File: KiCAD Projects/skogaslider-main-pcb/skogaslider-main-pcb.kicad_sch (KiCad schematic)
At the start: 183 parts, among them J1 USB_C_Receptacle_USB2.0, J2 USB_C_Receptacle_USB2.0, J3 Conn_01x03, J4 Conn_02x16_Top_Bottom, J5 HDMI_A_No_Video, J6 HDMI_A_No_Video, Q1 BSS138, SW1 SW_Push, SW2 SW_Push, SW3 SW_Push, SW4 SW_Push, U1 NCP1117-3.3_SOT223, U2 MPR121QR2, U3 MPR121QR2, U4 USBLC6-2P6, U5 RP2040, U6 M24C02-RMN, U7 W25Q128JVS, U8 MPR121QR2, U9 74HC4051, Y1 ABLS-12.000MHZ-B4-T

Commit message: New revision of the mainboard schematic and layout. Switched the air towers from HDMI to USB-C, and made them use the I2C bus for communication to reduce the number of pins
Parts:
- removed C57: 100nF, Capacitor_SMD:C_0402_1005Metric, symbol Device:C_Small
- removed H1, H10, H11, H12, H2, H3, H4, H5, H6, H7, H8, H9: MountingHole, MountingHole:MountingHole_3.2mm_M3, symbol Mechanical:MountingHole
- removed J5, J6: HDMI_A_No_Video, Skogaslider_Custom_Footprints:HDMI_Connector_SMD, symbol Skogaslider_Custom_Symbols:HDMI_A_No_Video
- removed R24: 10k, Resistor_SMD:R_0603_1608Metric, symbol Device:R
- removed SW1, SW2, SW3, SW4: SW_Push, TS-1187A-B-A-B:SW_TS-1187A-B-A-B, symbol Switch:SW_Push
- removed TP1, TP2, TP3, TP4: TestPoint, TestPoint:TestPoint_Pad_D1.5mm, symbol Connector:TestPoint
- removed U9: 74HC4051, Package_SO:TSSOP-16_4.4x5mm_P0.65mm, symbol 74xx:74HC4051
- added H1, H10, H2, H3, H4, H5, H6, H9: MountingHole_Pad, MountingHole:MountingHole_3.2mm_M3_DIN965_Pad_TopBottom, symbol Mechanical:MountingHole_Pad
- added J5, J6: USB_C_Receptacle_USB2.0, Connector_USB:USB_C_Receptacle_HRO_TYPE-C-31-M-12, symbol Connector:USB_C_Receptacle_USB2.0
- added S1: TS-1187A-B-A-B, TS-1187A-B-A-B:TS1187ABAB, symbol TS-1187A-B-A-B:TS-1187A-B-A-B
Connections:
- net +5V: now also R12.1, J5.A4 (VBUS), J5.A9 (VBUS), J5.B4 (VBUS), J5.B9 (VBUS), J6.A4 (VBUS), J6.A9 (VBUS), J6.B4 (VBUS), J6.B9 (VBUS)
- net GND: now also J5.A1 (GND), J5.A12 (GND), J5.B1 (GND), J5.B12 (GND), J5.S1 (SHIELD), J6.A1 (GND), J6.A12 (GND), J6.B1 (GND), J6.B12 (GND), J6.S1 (SHIELD), S1.C1 (NO_1), S1.D1 (NO_2)
- net RIGHT_RGB_DO: now also J5.A6 (D+), J5.B6 (D+), J6.A6 (D+), J6.B6 (D+)
- net SCL: now also J5.A5 (CC1), J5.B5 (CC2), J6.A5 (CC1), J6.B5 (CC2)
- net SDA: now also J5.A8 (SBU1), J5.B8 (SBU2), J6.A8 (SBU1), J6.B8 (SBU2)
- net SLIDER_RGB_DO: now also J6.A7 (D-), J6.B7 (D-)
- net ~{USB_BOOT}: now also S1.A1 (COM_1), S1.B1 (COM_2)
- net at D2.2 (A), J1.A4 (VBUS), J1.A9 (VBUS)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: no longer R12.1
- net AIR_LED_0: no longer names the net of U5.14 (GPIO11)
- net AIR_LED_1: no longer names the net of U5.17 (GPIO14)
- net AIR_LED_2: no longer names the net of U5.13 (GPIO10)
- net AIR_LED_3: no longer names the net of U5.16 (GPIO13)
- net AIR_LED_4: no longer names the net of U5.12 (GPIO9)
- net AIR_LED_5: no longer names the net of U5.15 (GPIO12)
- net AIR_SENSOR_IN: no longer names the net of U5.38 (GPIO26_ADC0)
- net MUX_0: no longer names the net of U5.27 (GPIO16)
- net MUX_1: no longer names the net of U5.28 (GPIO17)
- net MUX_2: no longer names the net of U5.29 (GPIO18)
- net SW_FUNCTION: no longer names the net of U5.11 (GPIO8)
- net SW_SVC: no longer names the net of U5.9 (GPIO7)
- net SW_TEST: no longer names the net of U5.8 (GPIO6)
- no-connect marks 36 -> 51
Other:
- note removed: "Air Sensor Multiplexer"
- note removed: "Function Buttons"
- moved on the sheet: C23, C24, D2, R12, R14, R23, Y1

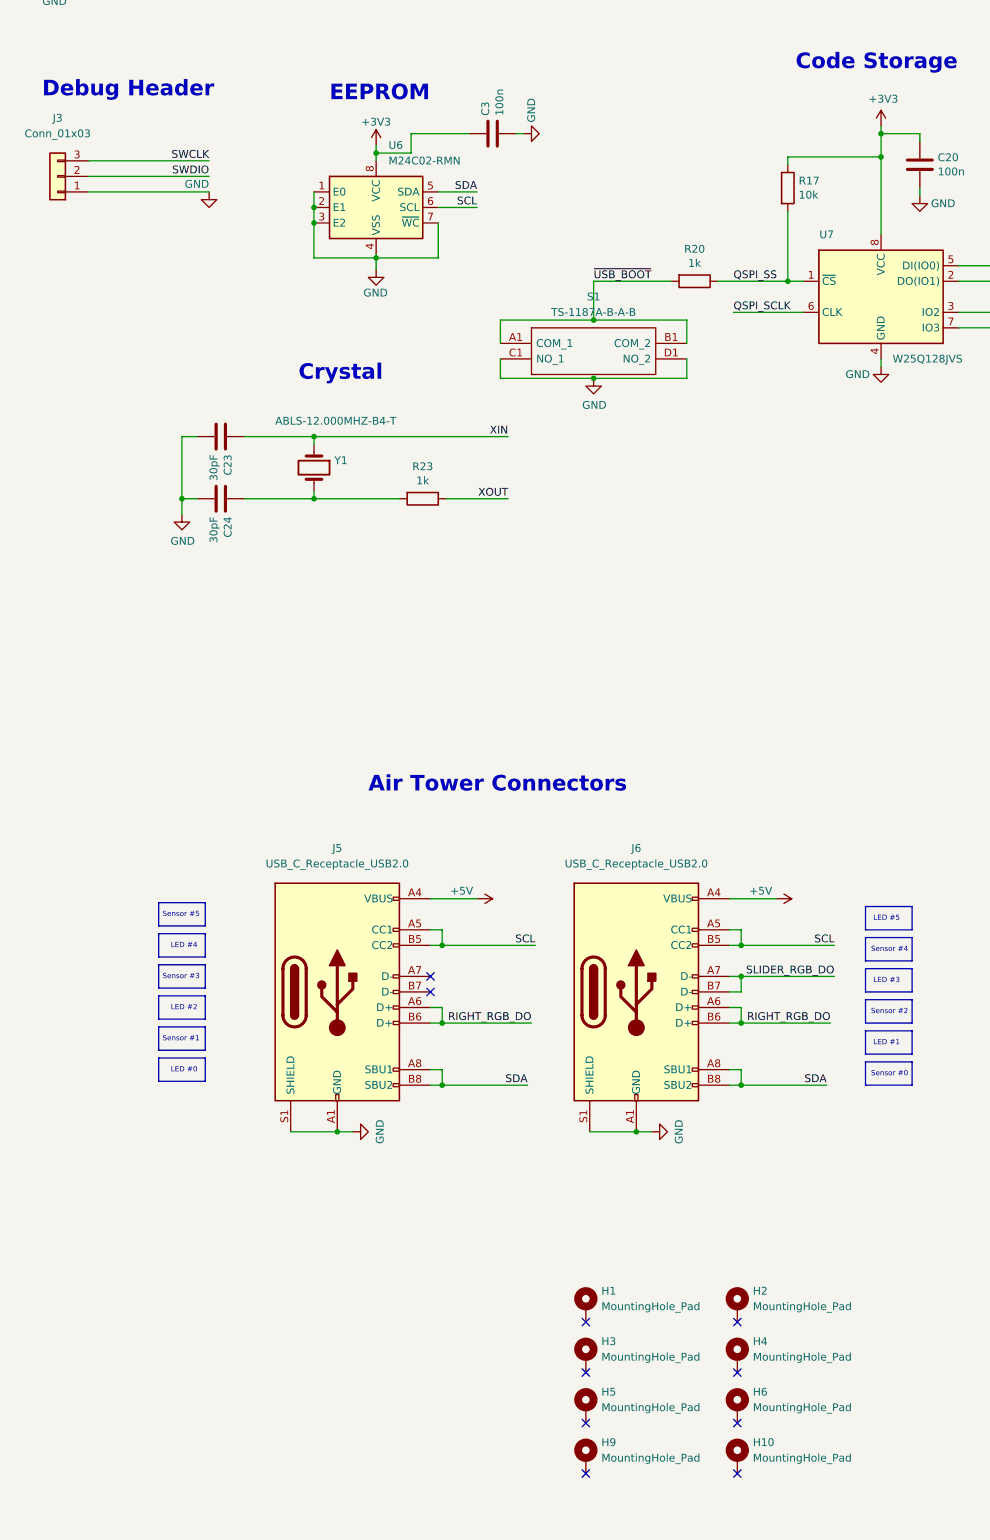
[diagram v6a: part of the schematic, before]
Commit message: Fix up the top edge of the board so it fits within the controller CAD, and add more mounting holes.
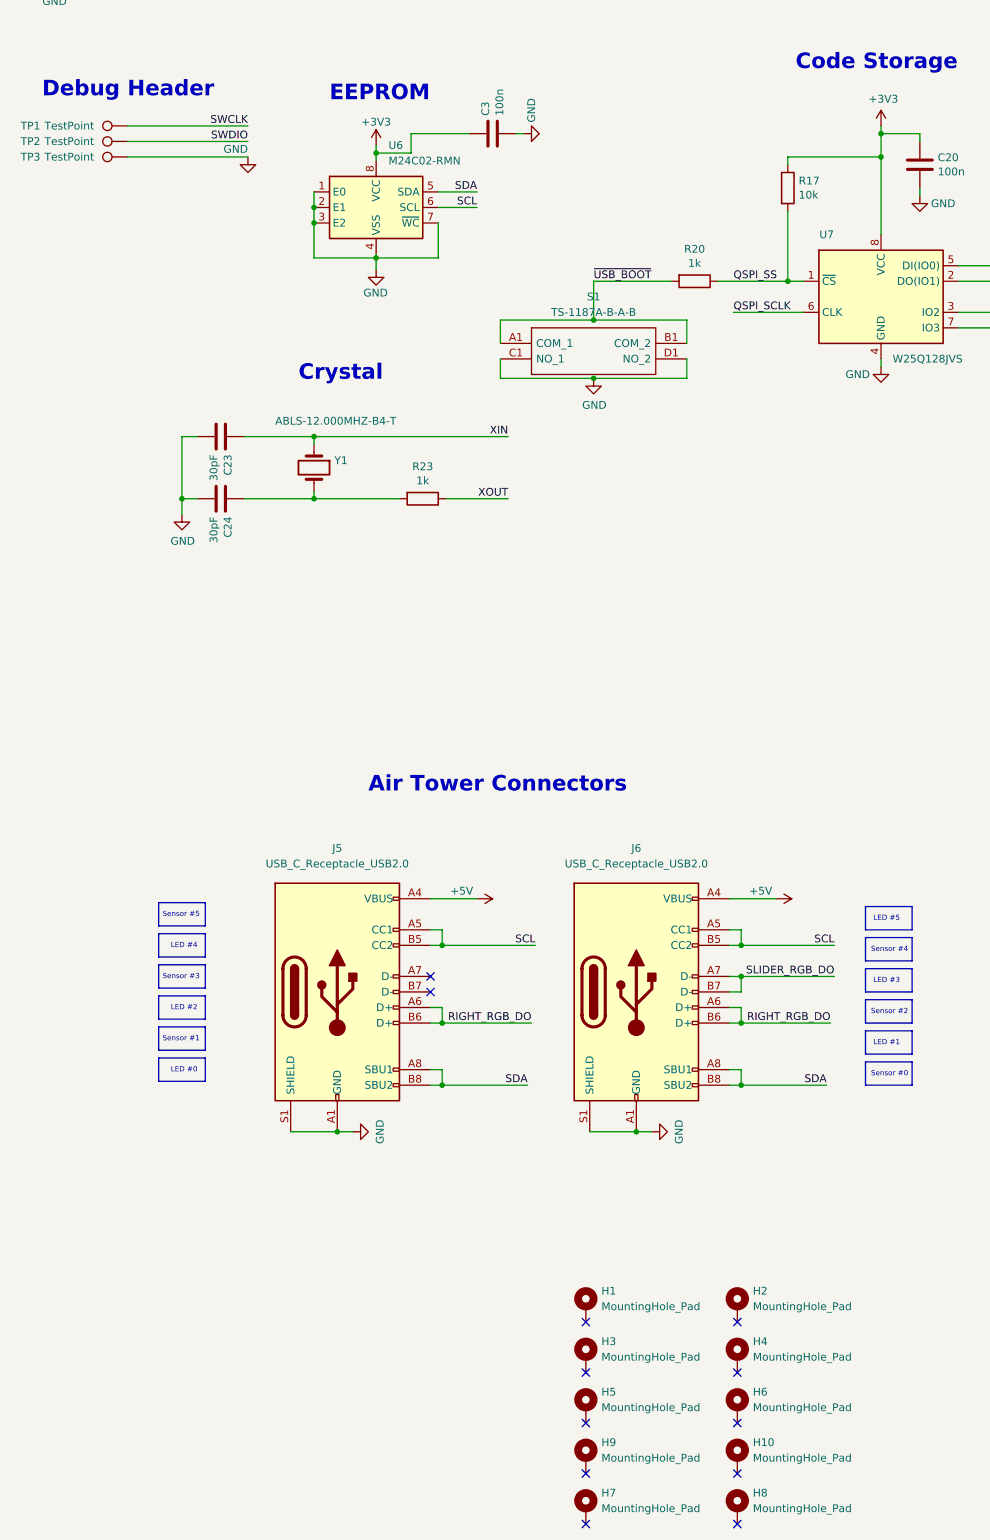
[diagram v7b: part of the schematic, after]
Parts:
- removed J3: Conn_01x03, Connector_PinHeader_2.54mm:PinHeader_1x03_P2.54mm_Vertical, symbol Connector_Generic:Conn_01x03
- added H7, H8: MountingHole_Pad, MountingHole:MountingHole_3.2mm_M3_DIN965_Pad_TopBottom, symbol Mechanical:MountingHole_Pad
- added TP1, TP2, TP3: TestPoint, TestPoint:TestPoint_Pad_1.0x1.0mm, symbol Connector:TestPoint
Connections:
- net GND: now also TP3.1
- net SWCLK: now also TP1.1
- net SWDIO: now also TP2.1
- no-connect marks 51 -> 53
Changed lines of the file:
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@@
   (no_connect (at 287.02 88.265))
   (no_connect (at 398.145 142.24))
+  (no_connect (at 109.22 341.63))
   (no_connect (at 399.415 63.5))
   (no_connect (at 134.62 53.975))
@@
   (no_connect (at 287.02 128.905))
   (no_connect (at 287.02 131.445))
+  (no_connect (at 133.985 341.63))
   (no_connect (at 487.045 63.5))
   (no_connect (at 133.985 308.61))
@@
     (stroke (width 0) (type default) (color 0 0 0 0))
   )
-  (wire (pts (xy 27.94 123.825) (xy 47.625 123.825))
+  (wire (pts (xy 34.29 118.11) (xy 53.975 118.11))
     (stroke (width 0) (type default) (color 0 0 0 0))
   )
@@
     (stroke (width 0) (type default) (color 0 0 0 0))
   )
-  (wire (pts (xy 27.94 118.745) (xy 47.625 118.745))
+  (wire (pts (xy 34.29 113.03) (xy 53.975 113.03))
     (stroke (width 0) (type default) (color 0 0 0 0))
   )
@@
     (stroke (width 0) (type default) (color 0 0 0 0))
   )
-  (wire (pts (xy 27.94 121.285) (xy 47.625 121.285))
+  (wire (pts (xy 34.29 115.57) (xy 53.975 115.57))
     (stroke (width 0) (type default) (color 0 0 0 0))
   )
@@
     (effects (font (size 1.27 1.27)) (justify right bottom))
   )
-  (label "SWCLK" (at 47.625 118.745 180)
+  (label "SWCLK" (at 53.975 113.03 180)
     (effects (font (size 1.27 1.27)) (justify right bottom))
   )
@@
     (effects (font (size 1.27 1.27)) (justify right bottom))
   )
-  (label "SWDIO" (at 47.625 121.285 180)
+  (label "SWDIO" (at 53.975 115.57 180)
     (effects (font (size 1.27 1.27)) (justify right bottom))
   )
@@
     (pin "2")
   )
-  (symbol (lib_id "power:GND") (at 47.625 123.825 0) (unit 1)
+  (symbol (lib_id "power:GND") (at 53.975 118.11 0) (unit 1)
     (in_bom yes) (on_board yes)
-    (property "Reference" "#PWR031" (id 0) (at 47.625 130.175 0)
+    (property "Reference" "#PWR031" (id 0) (at 53.975 124.46 0)
       (effects (font (size 1.27 1.27)) hide)
     )
-    (property "Value" "GND" (id 1) (at 47.625 122.555 0)
+    (property "Value" "GND" (id 1) (at 53.975 116.84 0)
       (effects (font (size 1.27 1.27)) (justify right))
     )
-    (property "Footprint" "" (id 2) (at 47.625 123.825 0)
+    (property "Footprint" "" (id 2) (at 53.975 118.11 0)
       (effects (font (size 1.27 1.27)) hide)
     )
-    (property "Datasheet" "" (id 3) (at 47.625 123.825 0)
+    (property "Datasheet" "" (id 3) (at 53.975 118.11 0)
       (effects (font (size 1.27 1.27)) hide)
     )
@@
     (pin "2")
   )
+  (symbol (lib_id "Connector:TestPoint") (at 34.29 115.57 90) (unit 1)
+    (in_bom yes) (on_board yes)
+    (property "Reference" "TP2" (id 0) (at 18.415 115.57 90))
+    (property "Value" "TestPoint" (id 1) (at 24.765 115.57 90))
+    (property "Footprint" "TestPoint:TestPoint_Pad_1.0x1.0mm" (id 2) (at 34.29 110.49 0)
+      (effects (font (size 1.27 1.27)) hide)
+    )
+    (property "Datasheet" "~" (id 3) (at 34.29 110.49 0)
+      (effects (font (size 1.27 1.27)) hide)
+    )
+    (pin "1")
+  )
   (symbol (lib_id "Device:C") (at 210.82 262.89 0) (unit 1)
     (in_bom yes) (on_board yes)
@@
     (pin "2")
   )
+  (symbol (lib_id "Connector:TestPoint") (at 34.29 118.11 90) (unit 1)
+    (in_bom yes) (on_board yes)
+    (property "Reference" "TP3" (id 0) (at 18.415 118.11 90))
+    (property "Value" "TestPoint" (id 1) (at 24.765 118.11 90))
+    (property "Footprint" "TestPoint:TestPoint_Pad_1.0x1.0mm" (id 2) (at 34.29 113.03 0)
+      (effects (font (size 1.27 1.27)) hide)
+    )
+    (property "Datasheet" "~" (id 3) (at 34.29 113.03 0)
+      (effects (font (size 1.27 1.27)) hide)
+    )
+    (pin "1")
+  )
   (symbol (lib_id "Device:C") (at 292.1 262.89 0) (unit 1)
     (in_bom yes) (on_board yes)
@@
     (pin "D1")
   )
+  (symbol (lib_id "Mechanical:MountingHole_Pad") (at 133.985 339.09 0) (unit 1)
+    (in_bom yes) (on_board yes) (fields_autoplaced)
+    (property "Reference" "H8" (id 0) (at 136.525 336.5499 0)
+      (effects (font (size 1.27 1.27)) (justify left))
+    )
+    (property "Value" "MountingHole_Pad" (id 1) (at 136.525 339.0899 0)
+      (effects (font (size 1.27 1.27)) (justify left))
+    )
+    (property "Footprint" "MountingHole:MountingHole_3.2mm_M3_DIN965_Pad_TopBottom" (id 2) (at 133.985 339.09 0)
+      (effects (font (size 1.27 1.27)) hide)
+    )
+    (property "Datasheet" "~" (id 3) (at 133.985 339.09 0)
+      (effects (font (size 1.27 1.27)) hide)
+    )
+    (pin "1")
+  )
   (symbol (lib_id "Device:C") (at 454.66 213.36 0) (unit 1)
     (in_bom yes) (on_board yes)
@@
     (pin "4")
   )
+  (symbol (lib_id "Mechanical:MountingHole_Pad") (at 109.22 339.09 0) (unit 1)
+    (in_bom yes) (on_board yes) (fields_autoplaced)
+    (property "Reference" "H7" (id 0) (at 111.76 336.5499 0)
+      (effects (font (size 1.27 1.27)) (justify left))
+    )
+    (property "Value" "MountingHole_Pad" (id 1) (at 111.76 339.0899 0)
+      (effects (font (size 1.27 1.27)) (justify left))
+    )
+    (property "Footprint" "MountingHole:MountingHole_3.2mm_M3_DIN965_Pad_TopBottom" (id 2) (at 109.22 339.09 0)
+      (effects (font (size 1.27 1.27)) hide)
+    )
+    (property "Datasheet" "~" (id 3) (at 109.22 339.09 0)
+      (effects (font (size 1.27 1.27)) hide)
+    )
+    (pin "1")
+  )
   (symbol (lib_id "Device:C") (at 414.02 213.36 0) (unit 1)
     (in_bom yes) (on_board yes)
@@
     (pin "2")
   )
+  (symbol (lib_id "Connector:TestPoint") (at 34.29 113.03 90) (unit 1)
+    (in_bom yes) (on_board yes)
+    (property "Reference" "TP1" (id 0) (at 18.415 113.03 90))
+    (property "Value" "TestPoint" (id 1) (at 24.765 113.03 90))
+    (property "Footprint" "TestPoint:TestPoint_Pad_1.0x1.0mm" (id 2) (at 34.29 107.95 0)
+      (effects (font (size 1.27 1.27)) hide)
+    )
+    (property "Datasheet" "~" (id 3) (at 34.29 107.95 0)
+      (effects (font (size 1.27 1.27)) hide)
+    )
+    (pin "1")
+  )
   (symbol (lib_id "Device:C") (at 353.06 238.125 0) (unit 1)
     (in_bom yes) (on_board yes)
@@
     (pin "1")
   )
-  (symbol (lib_id "Connector_Generic:Conn_01x03") (at 22.86 121.285 180) (unit 1)
-    (in_bom yes) (on_board yes) (fields_autoplaced)
-    (property "Reference" "J3" (id 0) (at 22.86 111.76 0))
-    (property "Value" "Conn_01x03" (id 1) (at 22.86 114.3 0))
-    (property "Footprint" "Connector_PinHeader_2.54mm:PinHeader_1x03_P2.54mm_Vertical" (id 2) (at 22.86 121.285 0)
-      (effects (font (size 1.27 1.27)) hide)
-    )
-    (property "Datasheet" "~" (id 3) (at 22.86 121.285 0)
-      (effects (font (size 1.27 1.27)) hide)
-    )
-    (pin "1")
-    (pin "2")
-    (pin "3")
-  )
   (symbol (lib_id "LED:WS2812B") (at 403.86 213.36 0) (unit 1)
     (in_bom yes) (on_board yes)
@@
       (reference "H6") (unit 1) (value "MountingHole_Pad") (footprint "MountingHole:MountingHole_3.2mm_M3_DIN965_Pad_TopBottom")
     )
+    (path "/a02d9b95-1c77-4b99-939b-46818c68dac8"
+      (reference "H7") (unit 1) (value "MountingHole_Pad") (footprint "MountingHole:MountingHole_3.2mm_M3_DIN965_Pad_TopBottom")
+    )
+    (path "/854adfe9-458e-47c7-9ed2-06ed6d88edbc"
+      (reference "H8") (unit 1) (value "MountingHole_Pad") (footprint "MountingHole:MountingHole_3.2mm_M3_DIN965_Pad_TopBottom")
+    )
     (path "/753493cd-9810-42af-b902-7ee9fec4039b"
       (reference "H9") (unit 1) (value "MountingHole_Pad") (footprint "MountingHole:MountingHole_3.2mm_M3_DIN965_Pad_TopBottom")
@@
       (reference "J2") (unit 1) (value "USB_C_Receptacle_USB2.0") (footprint "Connector_USB:USB_C_Receptacle_HRO_TYPE-C-31-M-12")
     )
-    (path "/ffae957e-b410-49bf-87b1-d9d7431025b7"
-      (reference "J3") (unit 1) (value "Conn_01x03") (footprint "Connector_PinHeader_2.54mm:PinHeader_1x03_P2.54mm_Vertical")
-    )
     (path "/b70bd8ca-551a-4823-83a6-3805f434b3a6"
       (reference "J4") (unit 1) (value "Conn_02x16_Top_Bottom") (footprint "Chunithm_Touch_Pad:Pads")
@@
       (reference "S1") (unit 1) (value "TS-1187A-B-A-B") (footprint "TS-1187A-B-A-B:TS1187ABAB")
     )
+    (path "/db449252-a7b8-46eb-91b2-601adf5f2652"
+      (reference "TP1") (unit 1) (value "TestPoint") (footprint "TestPoint:TestPoint_Pad_1.0x1.0mm")
+    )
+    (path "/3c31e52a-8775-4e73-8995-7f511af7b814"
+      (reference "TP2") (unit 1) (value "TestPoint") (footprint "TestPoint:TestPoint_Pad_1.0x1.0mm")
+    )
+    (path "/3dd42b8f-7f22-4ec3-812c-1dc359aabfbf"
+      (reference "TP3") (unit 1) (value "TestPoint") (footprint "TestPoint:TestPoint_Pad_1.0x1.0mm")
+    )
     (path "/6e876434-5eab-4277-9881-b9830566afba"
